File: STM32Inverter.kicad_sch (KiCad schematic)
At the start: 102 parts, among them J1 STLINK, J2 CURRENT SENSE, J5 UART, J6 INTERFACE, J7 POWER, J8 501571-2007, J9 RESOLVER, Q4 ST3422A, U1 STM32F303VCTx, U10 ULN2002, U11 LM393, U12 LM393, U4 74HCT00, U7 MCP2551-I-SN, Y3 CSTNE8M00GH5C000R0

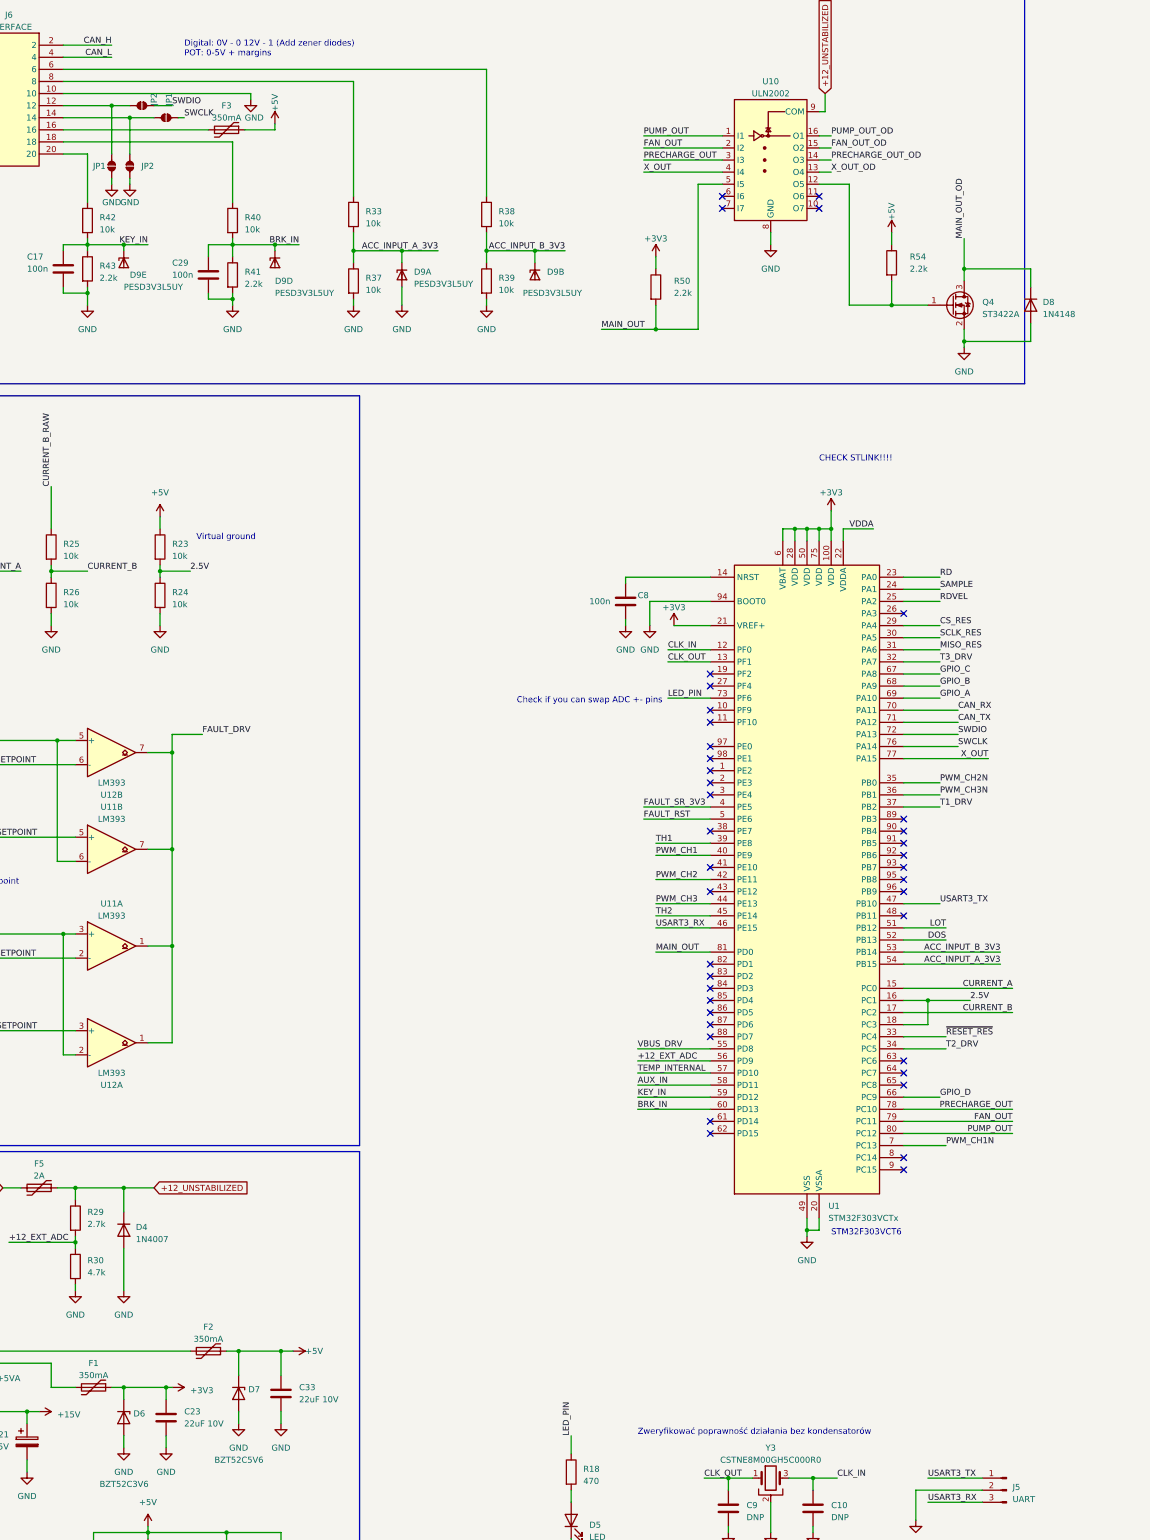
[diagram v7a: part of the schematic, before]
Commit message: Transistor temperature readout ok, vbus reading
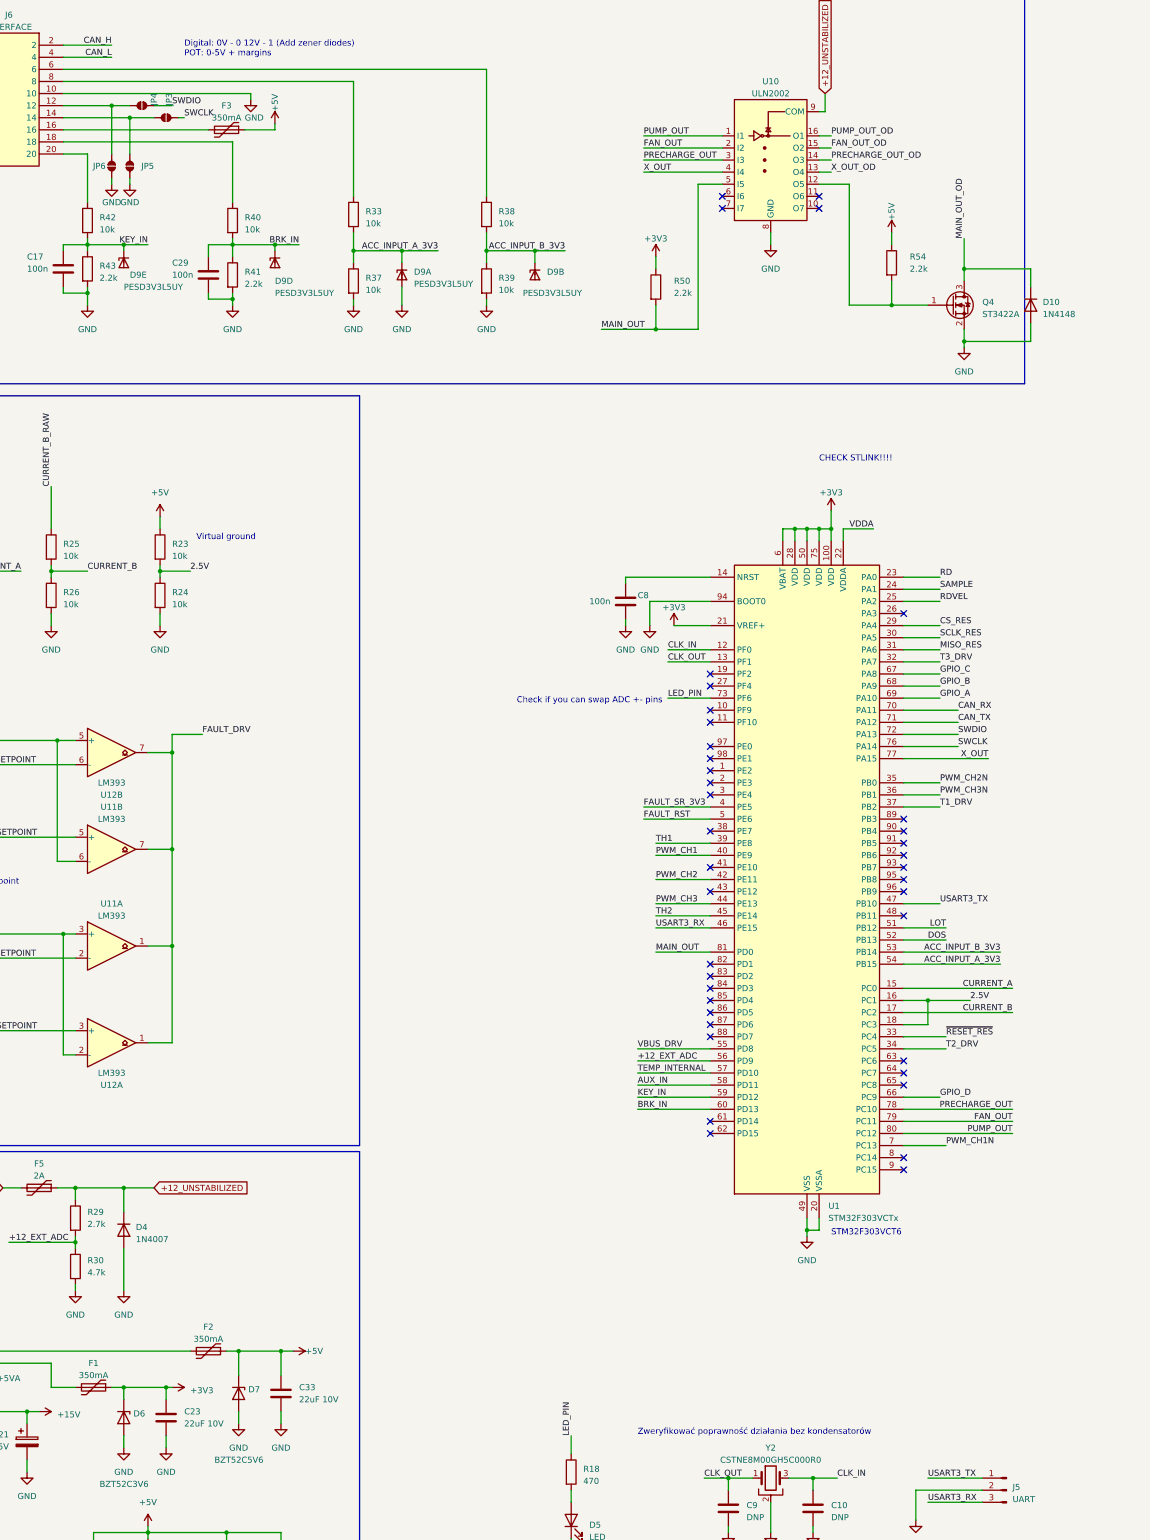
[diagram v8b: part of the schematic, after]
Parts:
- renumbered D8 to D10, JP1 to JP3, JP2 to JP4, JP2 to JP5, JP1 to JP6, Y3 to Y2
